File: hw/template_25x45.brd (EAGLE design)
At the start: 25 x 45 mm, 23 parts, among them J1 GROVE-4P-2.0-3470130P1, J2 GROVE-4P-2.0-3470130P1

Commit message: Small layout improvements
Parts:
- removed R3: 10k, rcl:R0603
- C1: value 1u -> (none)
- C9: value 10uF -> (none)
- U$6: value STM32F303C -> STM32F103CXTX
- moved R1 9.27 mm to (15.9, 7.70), turned to 90 degrees
- moved C6 4.00 mm to (22.7, 14.0)
- moved C17 1.40 mm to (22.7, 18.0)
- turned LED1 to 180 degrees
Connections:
- removed net BOOT0: R3.2, U$6.44
- net GND: now also LED1.C, U$6.44; no longer LED1.A, R3.1
- net LED1: now also U$6.6; no longer U$6.2
- net N$4: now also LED1.A; no longer LED1.C
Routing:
- net N$4: track 18.0 -> 4.61 mm, vias 2 -> 0
- net +3V3: track 86.7 -> 78.8 mm, vias 9 -> 7
- net LED1: track 2.90 -> 10.7 mm, vias 0 -> 2
- net BOOT0: track 3.84 -> 0.00 mm

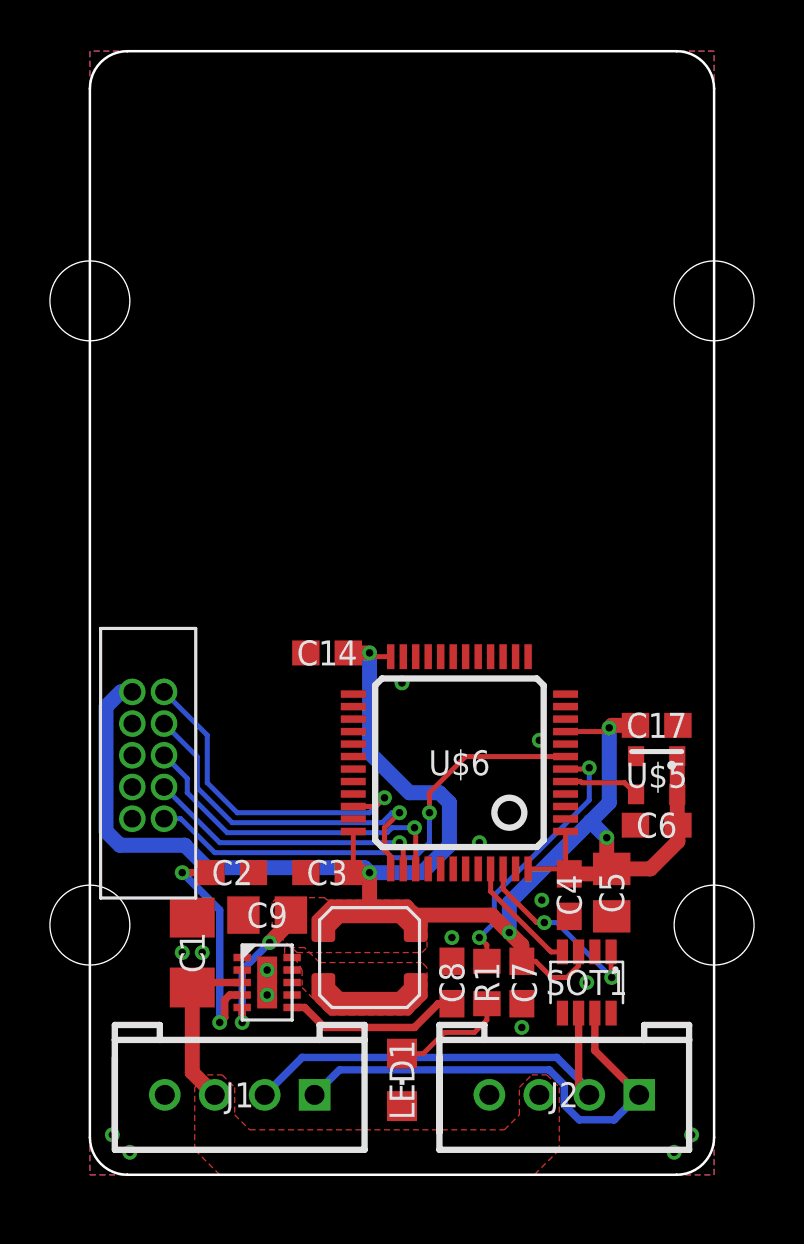
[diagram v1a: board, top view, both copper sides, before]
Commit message: Updated to R2P Eagle libraries
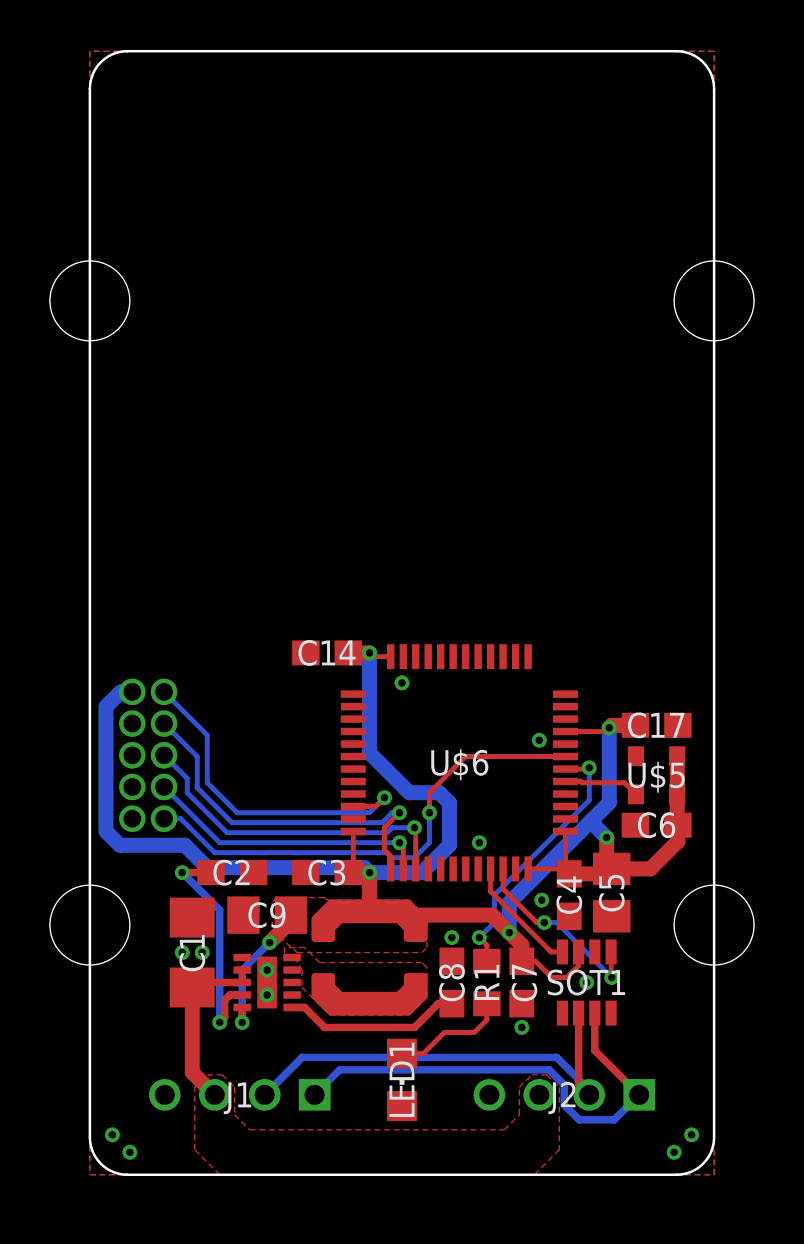
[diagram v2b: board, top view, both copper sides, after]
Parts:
- C1: value (none) -> 1u; device rcl:C1206 -> r2p_rcl:C1206
- C14, C17, C2, C3, C4, C6, C7, C8: device rcl:C0603 -> r2p_rcl:C0603
- C5: device rcl:C0805 -> r2p_rcl:C0805
- C9: value (none) -> 10u; device rcl:C0805 -> r2p_rcl:C0805
- J1, J2: value GROVE-4P-2.0-3470130P1 -> R2P_BUS-VERTICAL; device OPL Eagle Library:4P-2.0 -> r2p_connector:OPL-EAGLE-LIBRARY_4P-2.0
- LED1: device led:CHIPLED_0805 -> r2p_led:CHIPLED_0805
- R1: device rcl:R0603 -> r2p_rcl:R0603
- SOT1: device maxim:SOT23-8L -> r2p_ic:SOT23-8L
- U$2: device coilcraft:LPS4018 -> r2p_rcl:COILCRAFT_LPS4018
- U$3: device maxim:TDFN-10 -> r2p_ic:TDFN-10
- U$4: value FTSH-105TH -> JTAG-TH; device samtec:FTSH-105-TH -> r2p_connector:SAMTEC_FTSH-105-TH
- U$5: value ASD -> ABRACON_ASD; device abracon:2.5X2 -> r2p_ic:ABRACON_2.5X2
- U$6: value STM32F103CXTX -> STM32F303CTX; device st:LQFP48 -> r2p_ic:LQFP48
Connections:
- net VIN renamed +VBUS
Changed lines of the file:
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@@
 <layer number="54" name="bGND_GNDA" color="7" fill="1" visible="no" active="no"/>
 <layer number="56" name="wert" color="7" fill="1" visible="no" active="no"/>
+<layer number="90" name="Modules" color="5" fill="1" visible="no" active="no"/>
 <layer number="91" name="Nets" color="2" fill="1" visible="no" active="no"/>
 <layer number="92" name="Busses" color="1" fill="1" visible="no" active="no"/>
@@
 </autorouter>
 <elements>
-<element name="C6" library="rcl" package="C0603" value="10n" x="22.7" y="14" smashed="yes" rot="R180">
+<element name="C6" library="r2p_rcl" package="C0603" value="10n" x="22.7" y="14" smashed="yes" rot="R180">
 <attribute name="NAME" x="22.7" y="14" size="1" layer="25" font="vector" rot="R180" align="center"/>
 <attribute name="VALUE" x="23.335" y="15.905" size="1.27" layer="27" rot="R180"/>
 </element>
-<element name="C17" library="rcl" package="C0603" value="100n" x="22.7" y="18" smashed="yes">
+<element name="C17" library="r2p_rcl" package="C0603" value="100n" x="22.7" y="18" smashed="yes">
 <attribute name="NAME" x="22.7" y="18" size="1" layer="25" font="vector" align="center"/>
 <attribute name="VALUE" x="22.065" y="16.095" size="1.27" layer="27"/>
 </element>
-<element name="C14" library="rcl" package="C0603" value="100n" x="9.5" y="20.9" smashed="yes" rot="R180">
+<element name="C14" library="r2p_rcl" package="C0603" value="100n" x="9.5" y="20.9" smashed="yes" rot="R180">
 <attribute name="NAME" x="9.5" y="20.9" size="1" layer="25" font="vector" rot="R180" align="center"/>
 <attribute name="VALUE" x="10.135" y="22.805" size="1.27" layer="27" rot="R180"/>
 </element>
-<element name="C4" library="rcl" package="C0603" value="100n" x="19.2" y="11.2" smashed="yes" rot="R270">
+<element name="C4" library="r2p_rcl" package="C0603" value="100n" x="19.2" y="11.2" smashed="yes" rot="R270">
 <attribute name="NAME" x="19.2" y="11.2" size="1" layer="25" font="vector" rot="R270" align="center"/>
 <attribute name="VALUE" x="17.295" y="11.835" size="1.27" layer="27" rot="R270"/>
 </element>
-<element name="C5" library="rcl" package="C0805" value="4.7u" x="20.9" y="11.3" smashed="yes" rot="R270">
+<element name="C5" library="r2p_rcl" package="C0805" value="4.7u" x="20.9" y="11.3" smashed="yes" rot="R270">
 <attribute name="NAME" x="20.9" y="11.3" size="1" layer="25" font="vector" rot="R270" align="center"/>
 <attribute name="VALUE" x="18.36" y="12.57" size="1.27" layer="27" rot="R270"/>
 </element>
-<element name="C3" library="rcl" package="C0603" value="100n" x="9.5" y="12.1" smashed="yes" rot="R180">
+<element name="C3" library="r2p_rcl" package="C0603" value="100n" x="9.5" y="12.1" smashed="yes" rot="R180">
 <attribute name="NAME" x="9.5" y="12.1" size="1" layer="25" font="vector" rot="R180" align="center"/>
 <attribute name="VALUE" x="10.135" y="14.005" size="1.27" layer="27" rot="R180"/>
 </element>
-<element name="C7" library="rcl" package="C0603" value="100n" x="17.3" y="7.7" smashed="yes" rot="R270">
+<element name="C7" library="r2p_rcl" package="C0603" value="100n" x="17.3" y="7.7" smashed="yes" rot="R270">
 <attribute name="NAME" x="17.4" y="7.7" size="1" layer="25" font="vector" rot="R270" align="center"/>
 <attribute name="VALUE" x="15.395" y="8.335" size="1.27" layer="27" rot="R270"/>
 </element>
-<element name="LED1" library="led" package="CHIPLED_0805" value="" x="12.5" y="3.8" smashed="yes" rot="R180">
+<element name="LED1" library="r2p_led" package="CHIPLED_0805" value="" x="12.5" y="3.8" smashed="yes" rot="R180">
 <attribute name="NAME" x="12.5" y="3.8" size="1" layer="25" font="vector" rot="R270" align="center"/>
 <attribute name="VALUE" x="9.96" y="5.07" size="1.27" layer="27" rot="R270"/>
 </element>
-<element name="R1" library="rcl" package="R0603" value="330" x="15.9" y="7.7" smashed="yes" rot="R90">
+<element name="R1" library="r2p_rcl" package="R0603" value="330" x="15.9" y="7.7" smashed="yes" rot="R90">
 <attribute name="NAME" x="15.9" y="7.7" size="1" layer="25" font="vector" rot="R90" align="center"/>
 <attribute name="VALUE" x="17.805" y="7.065" size="1.27" layer="27" rot="R90"/>
 </element>
-<element name="U$4" library="samtec" package="FTSH-105-TH" value="FTSH-105TH" x="1.7" y="16.8" smashed="yes" rot="R270"/>
-<element name="J2" library="OPL Eagle Library" package="4P-2.0" value="GROVE-4P-2.0-3470130P1" x="19" y="3.2" smashed="yes" rot="R180">
+<element name="U$4" library="r2p_connector" package="SAMTEC_FTSH-105-TH" value="JTAG-TH" x="1.7" y="16.8" smashed="yes" rot="R270"/>
+<element name="J2" library="r2p_connector" package="OPL-EAGLE-LIBRARY_4P-2.0" value="R2P_BUS-VERTICAL" x="19" y="3.2" smashed="yes" rot="R180">
 <attribute name="NAME" x="19" y="3.2" size="1" layer="25" font="vector" ratio="11" rot="R180" align="center"/>
 <attribute name="VALUE" x="20.905" y="3.2" size="0.635" layer="27" font="vector" ratio="10" rot="R180"/>
 </element>
-<element name="U$2" library="coilcraft" package="LPS4018" value="LPS4018" x="11.2" y="8.7" smashed="yes" rot="R90"/>
-<element name="C1" library="rcl" package="C1206" value="" x="4.1" y="8.9" smashed="yes" rot="R90">
+<element name="U$2" library="r2p_rcl" package="COILCRAFT_LPS4018" value="LPS4018" x="11.2" y="8.7" smashed="yes" rot="R90"/>
+<element name="C1" library="r2p_rcl" package="C1206" value="1u" x="4.1" y="8.9" smashed="yes" rot="R90">
 <attribute name="NAME" x="4.1" y="8.9" size="1" layer="25" font="vector" rot="R90" align="center"/>
 <attribute name="VALUE" x="6.64" y="7.63" size="1.27" layer="27" rot="R90"/>
 </element>
-<element name="C2" library="rcl" package="C0603" value="1u" x="5.7" y="12.1" smashed="yes">
+<element name="C2" library="r2p_rcl" package="C0603" value="1u" x="5.7" y="12.1" smashed="yes">
 <attribute name="NAME" x="5.7" y="12.1" size="1" layer="25" font="vector" align="center"/>
 <attribute name="VALUE" x="5.065" y="10.195" size="1.27" layer="27"/>
 </element>
-<element name="C8" library="rcl" package="C0603" value="10n" x="14.5" y="7.7" smashed="yes" rot="R90">
+<element name="C8" library="r2p_rcl" package="C0603" value="10n" x="14.5" y="7.7" smashed="yes" rot="R90">
 <attribute name="NAME" x="14.5" y="7.7" size="1" layer="25" font="vector" rot="R90" align="center"/>
 <attribute name="VALUE" x="16.405" y="7.065" size="1.27" layer="27" rot="R90"/>
 </element>
-<element name="C9" library="rcl" package="C0805" value="" x="7.1" y="10.4" smashed="yes" rot="R180">
+<element name="C9" library="r2p_rcl" package="C0805" value="10u" x="7.1" y="10.4" smashed="yes" rot="R180">
 <attribute name="NAME" x="7.1" y="10.4" size="1" layer="25" font="vector" rot="R180" align="center"/>
 <attribute name="VALUE" x="8.37" y="12.94" size="1.27" layer="27" rot="R180"/>
 </element>
-<element name="U$3" library="maxim" package="TDFN-10" value="MAX17501" x="7.1" y="7.7" smashed="yes"/>
-<element name="J1" library="OPL Eagle Library" package="4P-2.0" value="GROVE-4P-2.0-3470130P1" x="6" y="3.2" smashed="yes" rot="R180">
+<element name="U$3" library="r2p_ic" package="TDFN-10" value="MAX17501" x="7.1" y="7.7" smashed="yes"/>
+<element name="J1" library="r2p_connector" package="OPL-EAGLE-LIBRARY_4P-2.0" value="R2P_BUS-VERTICAL" x="6" y="3.2" smashed="yes" rot="R180">
 <attribute name="NAME" x="6" y="3.2" size="1" layer="25" font="vector" ratio="11" rot="R180" align="center"/>
 <attribute name="VALUE" x="7.905" y="3.2" size="0.635" layer="27" font="vector" ratio="10" rot="R180"/>
 </element>
-<element name="U$6" library="st" package="LQFP48" value="STM32F103CXTX" x="14.8" y="16.5" smashed="yes" rot="R180">
+<element name="U$6" library="r2p_ic" package="LQFP48" value="STM32F303CTX" x="14.8" y="16.5" smashed="yes" rot="R180">
 <attribute name="NAME" x="14.8" y="16.5" size="1" layer="25" font="vector" rot="R180" align="center"/>
 <attribute name="VALUE" x="17.34" y="19.04" size="1.27" layer="27" rot="R180"/>
 </element>
-<element name="SOT1" library="maxim" package="SOT23-8L" value="MAX3051EKA" x="19.9" y="7.7" smashed="yes" rot="R180">
+<element name="SOT1" library="r2p_ic" package="SOT23-8L" value="MAX3051EKA" x="19.9" y="7.7" smashed="yes" rot="R180">
 <attribute name="NAME" x="19.9" y="7.7" size="1" layer="25" font="vector" rot="R180" align="center"/>
 <attribute name="VALUE" x="16.725" y="9.605" size="1.27" layer="27" rot="R270"/>
 </element>
 <element name="U$1" library="r2p_pcb" package="25X45" value="PCB_25X45" x="0" y="0" smashed="yes"/>
-<element name="U$5" library="abracon" package="2.5X2" value="ASD" x="22.7" y="16" smashed="yes" rot="R180">
+<element name="U$5" library="r2p_ic" package="ABRACON_2.5X2" value="ABRACON_ASD" x="22.7" y="16" smashed="yes" rot="R180">
 <attribute name="NAME" x="22.7" y="16" size="1" layer="25" font="vector" rot="R180" align="center"/>
 <attribute name="VALUE" x="24.95" y="18.75" size="1.27" layer="27" rot="R180"/>
@@
 <via x="15.6" y="13.3" extent="1-16" drill="0.3"/>
 </signal>
-<signal name="VIN">
+<signal name="+VBUS">
 <contactref element="J1" pad="3"/>
 <contactref element="C1" pad="1"/>

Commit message: Updated keepout
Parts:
- U$2: value LPS4018 -> (none)
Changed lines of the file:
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@@
 <attribute name="VALUE" x="20.905" y="3.2" size="0.635" layer="27" font="vector" ratio="10" rot="R180"/>
 </element>
-<element name="U$2" library="r2p_rcl" package="COILCRAFT_LPS4018" value="LPS4018" x="11.2" y="8.7" smashed="yes" rot="R90"/>
+<element name="U$2" library="r2p_rcl" package="COILCRAFT_LPS4018" value="" x="11.2" y="8.7" smashed="yes" rot="R90"/>
 <element name="C1" library="r2p_rcl" package="C1206" value="1u" x="4.1" y="8.9" smashed="yes" rot="R90">
 <attribute name="NAME" x="4.1" y="8.9" size="1" layer="25" font="vector" rot="R90" align="center"/>
